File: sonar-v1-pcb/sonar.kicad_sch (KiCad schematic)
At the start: 14 parts, among them J1 DF40C-80DS-0.4V51, U1 XT60_M

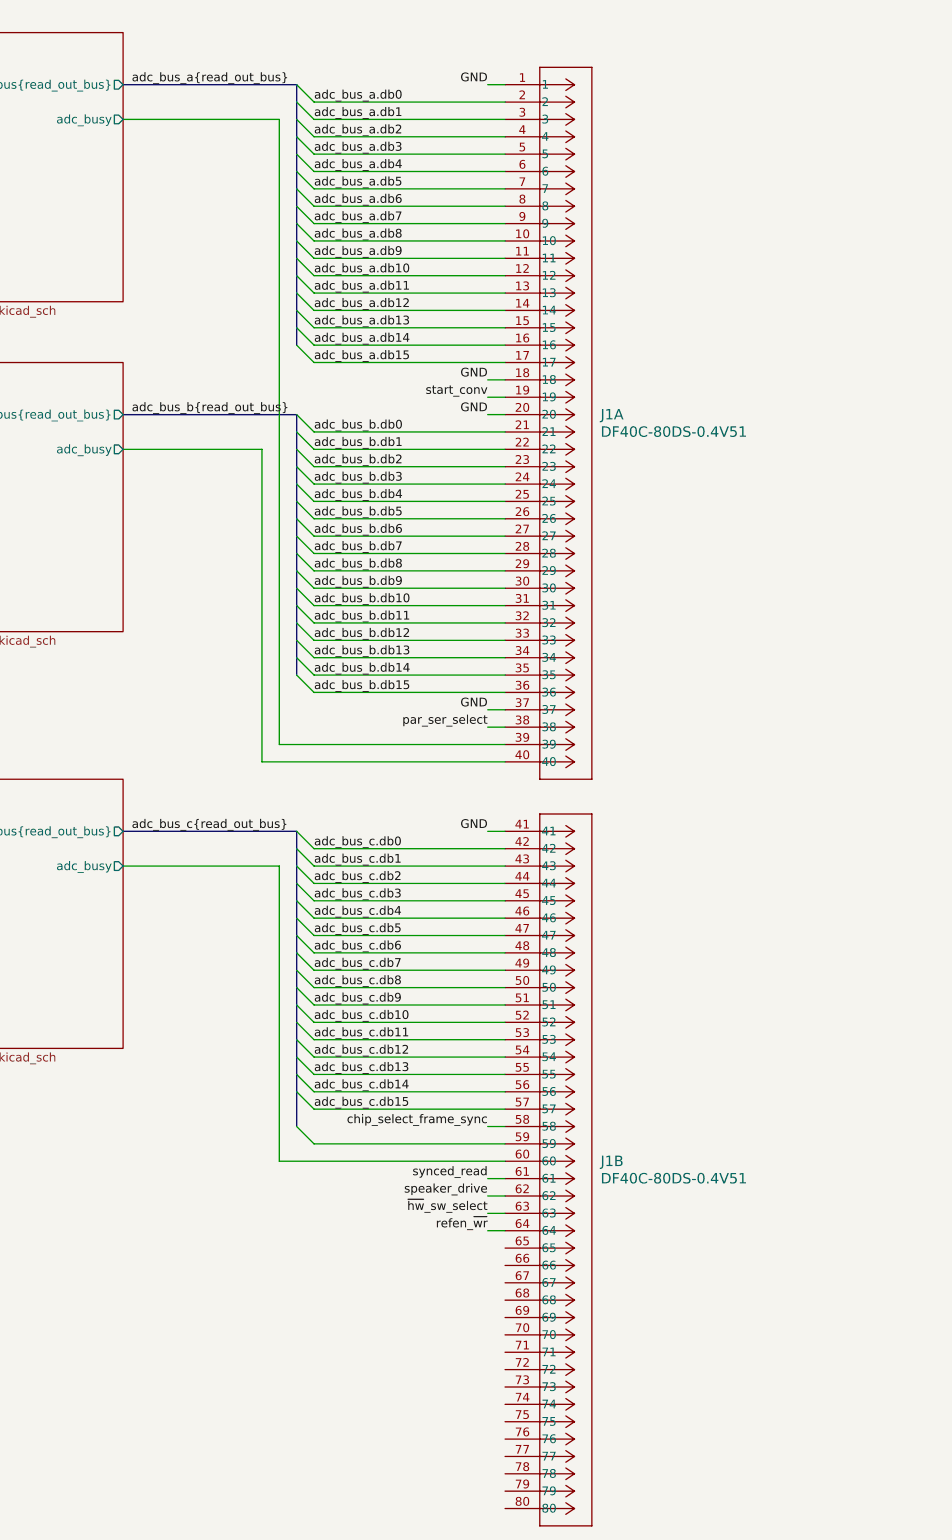
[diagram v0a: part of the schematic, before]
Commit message: T-011: digital sheet, authoritative pinmap.md, generator; top-sheet adc_bus removal
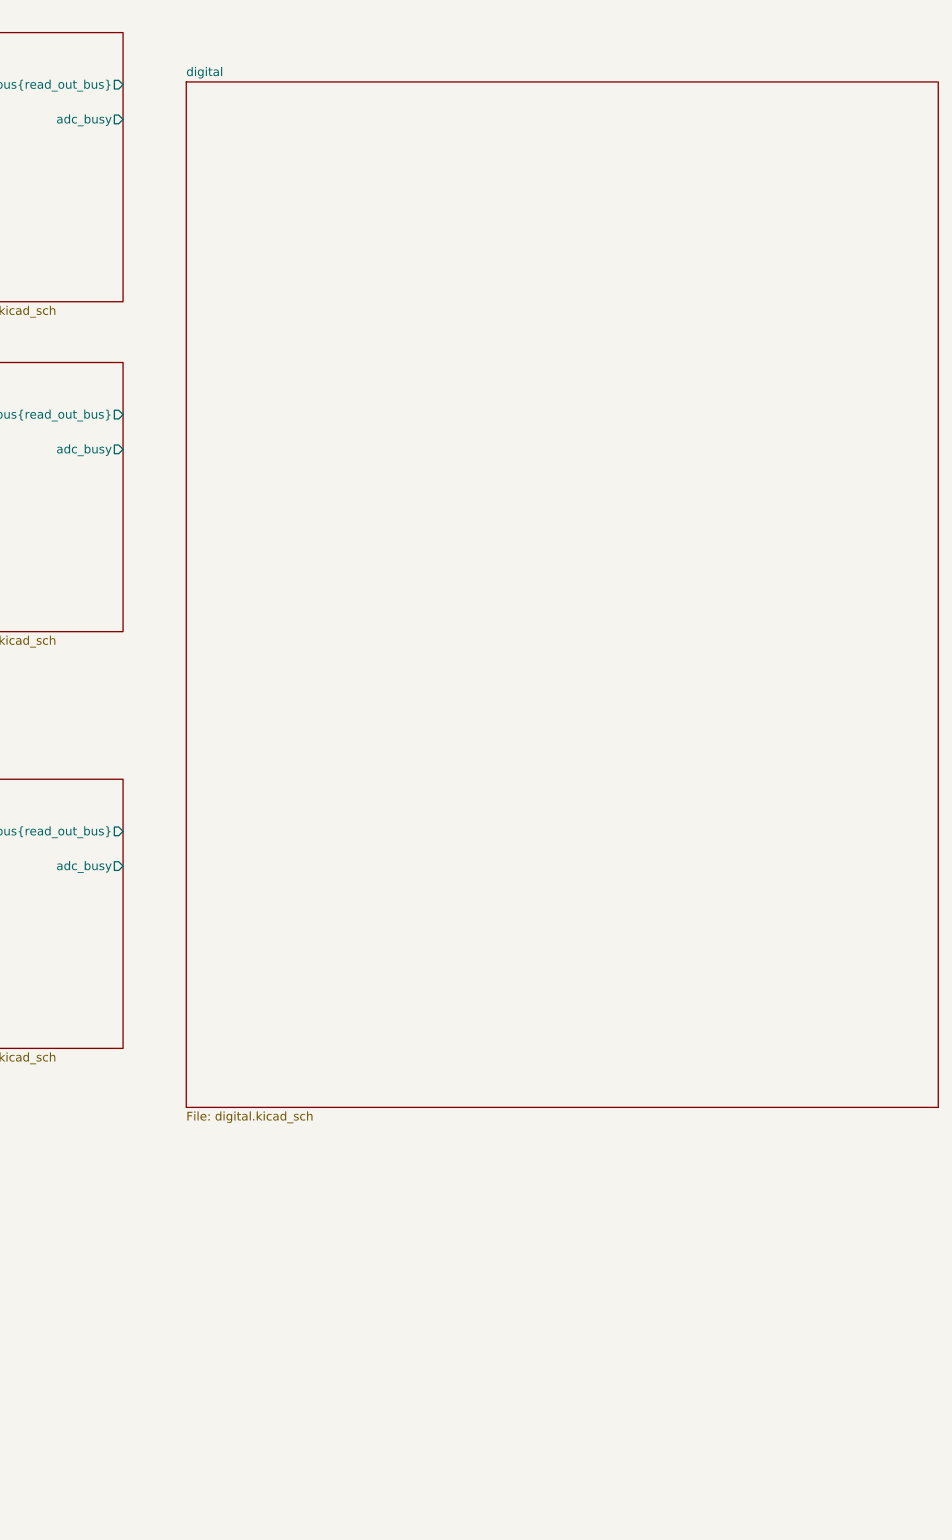
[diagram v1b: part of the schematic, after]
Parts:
- removed J1: DF40C-80DS-0.4V51, CONN80_DF40C-80DS_HIR, symbol sonar_lib:DF40C-80DS-0.4V51
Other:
- added sheet digital (digital.kicad_sch)

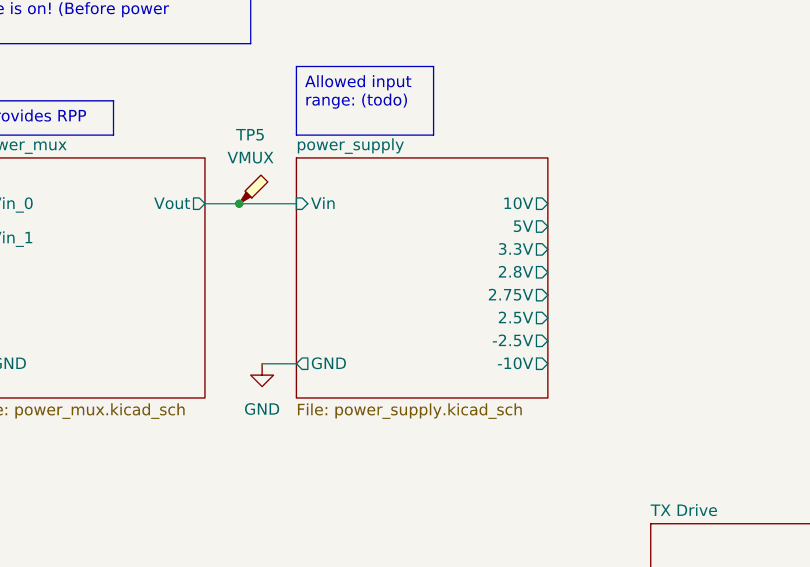
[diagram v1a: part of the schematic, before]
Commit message: T-012: prune power tree to four rails (drop 6 legacy sheets, rewire supply/top)
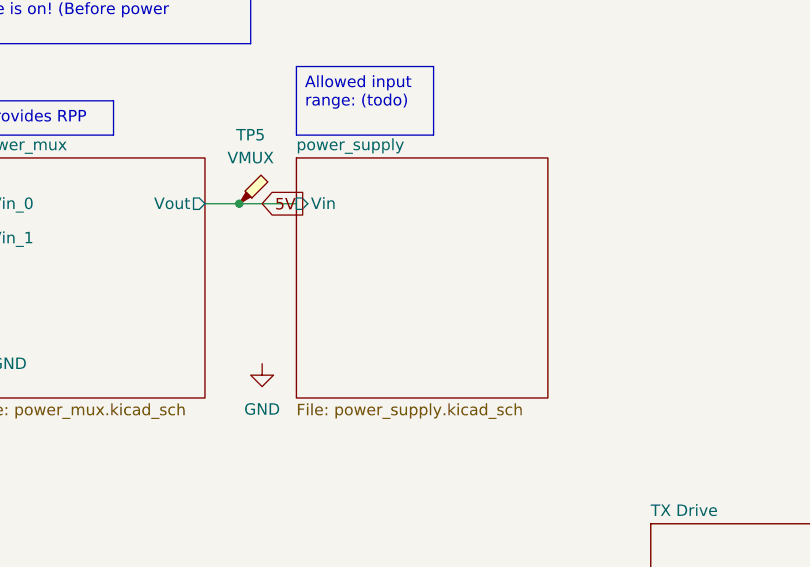
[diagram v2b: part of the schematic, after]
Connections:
- net power_mux/Vout renamed 5V
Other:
- sheet power_supply ports: added none; removed -10V, -2.5V, 10V, 2.5V, 2.75V, 2.8V, 3.3V, 5V, GND
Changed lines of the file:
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@@
-	(wire
-		(pts
-			(xy 138.43 147.32) (xy 142.24 147.32)
-		)
-		(stroke
-			(width 0)
-			(type default)
-		)
-	)
 	(wire
 		(pts
@@
 		)
 	)
+	(global_label "5V"
+		(shape input)
+		(at 138.43 129.54 0)
+		(effects
+			(font
+				(size 1.27 1.27)
+			)
+			(justify left)
+		)
+		(fields_autoplaced yes)
+	)
 	(sheet
 		(at 142.24 124.46)
@@
 			)
 		)
-		(pin "GND" output
-			(at 142.24 147.32 180)
-			(effects
-				(font
-					(size 1.27 1.27)
-				)
-				(justify left)
-			)
-		)
-		(pin "3.3V" output
-			(at 170.18 134.62 0)
-			(effects
-				(font
-					(size 1.27 1.27)
-				)
-				(justify right)
-			)
-		)
-		(pin "10V" output
-			(at 170.18 129.54 0)
-			(effects
-				(font
-					(size 1.27 1.27)
-				)
-				(justify right)
-			)
-		)
-		(pin "2.75V" output
-			(at 170.18 139.7 0)
-			(effects
-				(font
-					(size 1.27 1.27)
-				)
-				(justify right)
-			)
-		)
-		(pin "-10V" output
-			(at 170.18 147.32 0)
-			(effects
-				(font
-					(size 1.27 1.27)
-				)
-				(justify right)
-			)
-		)
-		(pin "5V" output
-			(at 170.18 132.08 0)
-			(effects
-				(font
-					(size 1.27 1.27)
-				)
-				(justify right)
-			)
-		)
-		(pin "2.5V" output
-			(at 170.18 142.24 0)
-			(effects
-				(font
-					(size 1.27 1.27)
-				)
-				(justify right)
-			)
-		)
-		(pin "-2.5V" output
-			(at 170.18 144.78 0)
-			(effects
-				(font
-					(size 1.27 1.27)
-				)
-				(justify right)
-			)
-		)
-		(pin "2.8V" output
-			(at 170.18 137.16 0)
-			(effects
-				(font
-					(size 1.27 1.27)
-				)
-				(justify right)
-			)
-		)

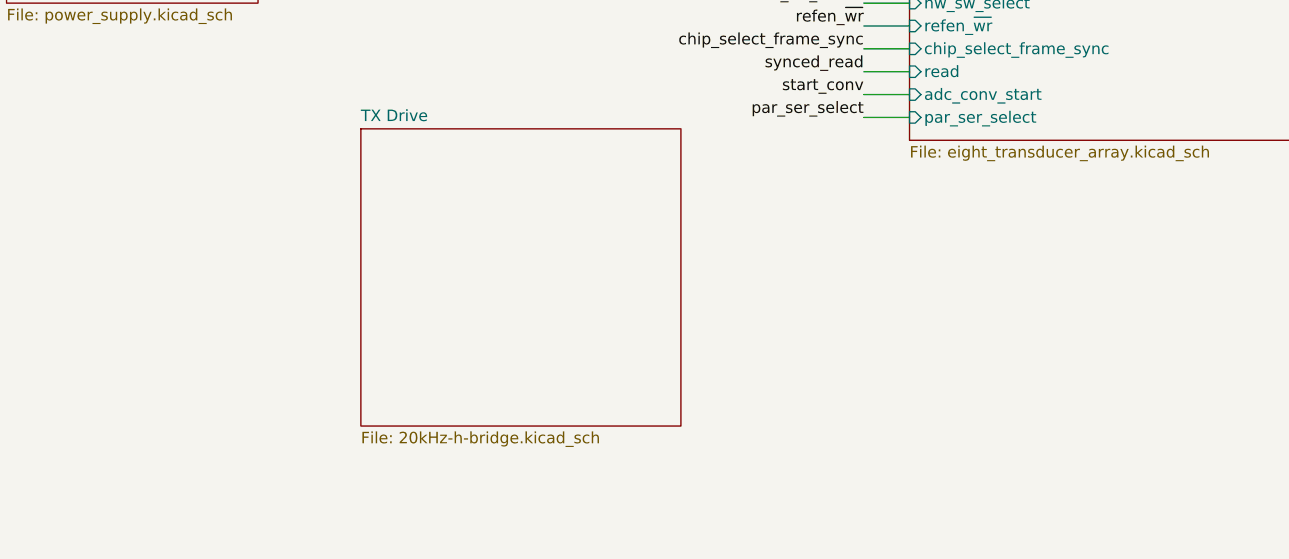
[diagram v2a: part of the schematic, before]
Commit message: T-013: hook up DRV8876 h-bridge, off-board TX connector, C6 dup-ref fix
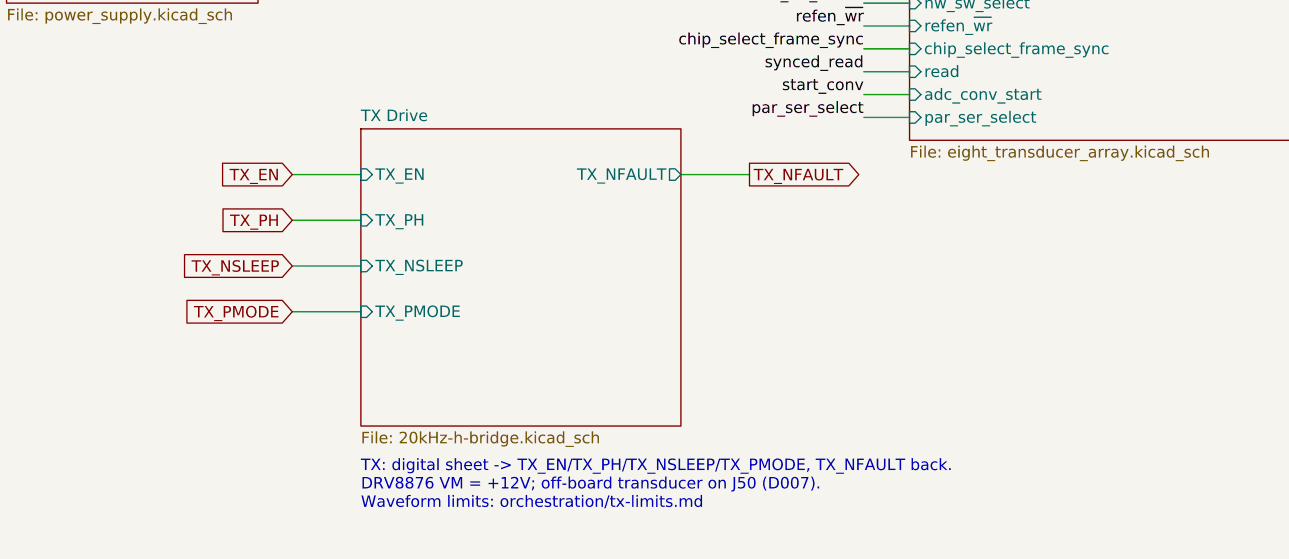
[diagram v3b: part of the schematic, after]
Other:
- sheet TX Drive ports: added TX_EN, TX_NFAULT, TX_NSLEEP, TX_PH, TX_PMODE; removed none
- note added: "TX: digital sheet -> TX_EN/TX_PH/TX_NSLEEP/TX_PMODE, TX_NFAULT back. DRV8876 VM = +12V; off-board transducer on J50 (D007). Waveform limits: orchestration/tx-limits.md"
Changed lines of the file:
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@@
+			)
+		)
+		(pin "TX_EN" input
+			(at 181.61 170.18 180)
+			(effects
+				(font
+					(size 1.27 1.27)
+				)
+				(justify left)
+			)
+		)
+		(pin "TX_PH" input
+			(at 181.61 175.26 180)
+			(effects
+				(font
+					(size 1.27 1.27)
+				)
+				(justify left)
+			)
+		)
+		(pin "TX_NSLEEP" input
+			(at 181.61 180.34 180)
+			(effects
+				(font
+					(size 1.27 1.27)
+				)
+				(justify left)
+			)
+		)
+		(pin "TX_PMODE" input
+			(at 181.61 185.42 180)
+			(effects
+				(font
+					(size 1.27 1.27)
+				)
+				(justify left)
+			)
+		)
+		(pin "TX_NFAULT" output
+			(at 217.17 170.18 0)
+			(effects
+				(font
+					(size 1.27 1.27)
+				)
+				(justify right)
 			)
 		)
@@
 		)
 	)
+	(wire
+		(pts
+			(xy 181.61 170.18) (xy 173.99 170.18)
+		)
+		(stroke
+			(width 0)
+			(type default)
+		)
+	)
+	(global_label "TX_EN"
+		(shape input)
+		(at 173.99 170.18 180)
+		(effects
+			(font
+				(size 1.27 1.27)
+			)
+			(justify right)
+		)
+		(property "Intersheetrefs" "${INTERSHEET_REFS}"
+			(at 173.99 170.18 0)
+			(effects
+				(font
+					(size 1.27 1.27)
+				)
+				(hide yes)
+			)
+		)
+	)
+	(wire
+		(pts
+			(xy 181.61 175.26) (xy 173.99 175.26)
+		)
+		(stroke
+			(width 0)
+			(type default)
+		)
+	)
+	(global_label "TX_PH"
+		(shape input)
+		(at 173.99 175.26 180)
+		(effects
+			(font
+				(size 1.27 1.27)
+			)
+			(justify right)
+		)
+		(property "Intersheetrefs" "${INTERSHEET_REFS}"
+			(at 173.99 175.26 0)
+			(effects
+				(font
+					(size 1.27 1.27)
+				)
+				(hide yes)
+			)
+		)
+	)
+	(wire
+		(pts
+			(xy 181.61 180.34) (xy 173.99 180.34)
+		)
+		(stroke
+			(width 0)
+			(type default)
+		)
+	)
+	(global_label "TX_NSLEEP"
+		(shape input)
+		(at 173.99 180.34 180)
+		(effects
+			(font
+				(size 1.27 1.27)
+			)
+			(justify right)
+		)
+		(property "Intersheetrefs" "${INTERSHEET_REFS}"
+			(at 173.99 180.34 0)
+			(effects
+				(font
+					(size 1.27 1.27)
+				)
+				(hide yes)
+			)
+		)
+	)
+	(wire
+		(pts
+			(xy 181.61 185.42) (xy 173.99 185.42)
+		)
+		(stroke
+			(width 0)
+			(type default)
+		)
+	)
+	(global_label "TX_PMODE"
+		(shape input)
+		(at 173.99 185.42 180)
+		(effects
+			(font
+				(size 1.27 1.27)
+			)
+			(justify right)
+		)
+		(property "Intersheetrefs" "${INTERSHEET_REFS}"
+			(at 173.99 185.42 0)
+			(effects
+				(font
+					(size 1.27 1.27)
+				)
+				(hide yes)
+			)
+		)
+	)
+	(wire
+		(pts
+			(xy 217.17 170.18) (xy 224.79 170.18)
+		)
+		(stroke
+			(width 0)
+			(type default)
+		)
+	)
+	(global_label "TX_NFAULT"
+		(shape output)
+		(at 224.79 170.18 0)
+		(effects
+			(font
+				(size 1.27 1.27)
+			)
+			(justify left)
+		)
+		(property "Intersheetrefs" "${INTERSHEET_REFS}"
+			(at 224.79 170.18 0)
+			(effects
+				(font
+					(size 1.27 1.27)
+				)
+				(hide yes)
+			)
+		)
+	)
+	(text "TX: digital sheet -> TX_EN/TX_PH/TX_NSLEEP/TX_PMODE, TX_NFAULT back.\nDRV8876 VM = +12V; off-board transducer on J50 (D007).\nWaveform limits: orchestration/tx-limits.md"
+		(exclude_from_sim no)
+		(at 181.61 201.93 0)
+		(effects
+			(font
+				(size 1.27 1.27)
+			)
+			(justify left top)
+		)
+	)
